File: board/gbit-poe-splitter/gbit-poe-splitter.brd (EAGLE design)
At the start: 100 x 80 mm, 51 parts, among them IC1 LM2596HVS, U1 TPS2379DDA

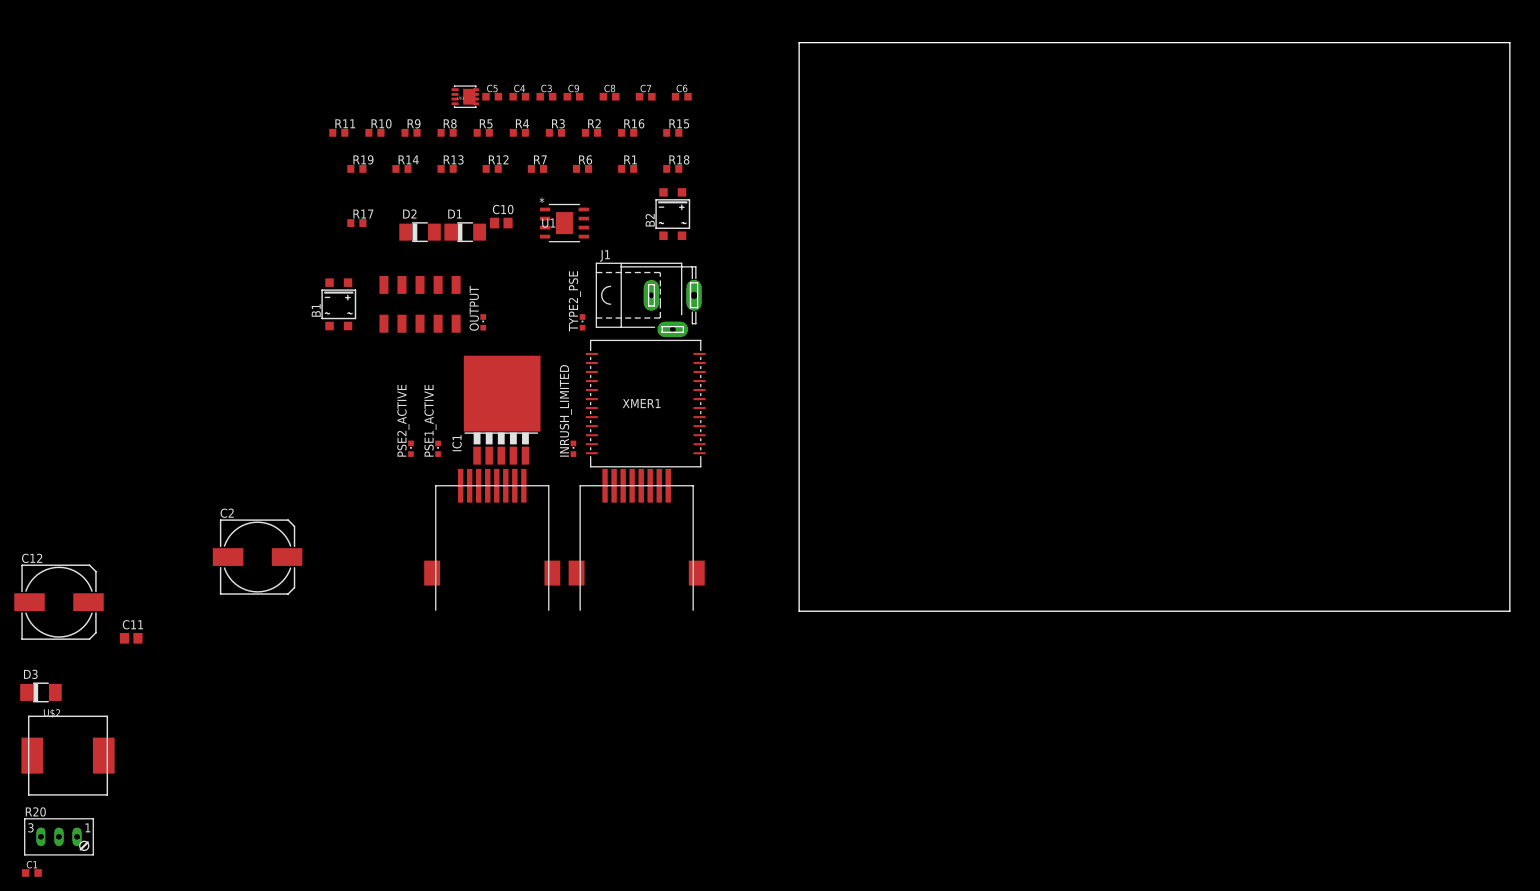
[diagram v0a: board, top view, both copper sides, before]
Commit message: Began the routing process
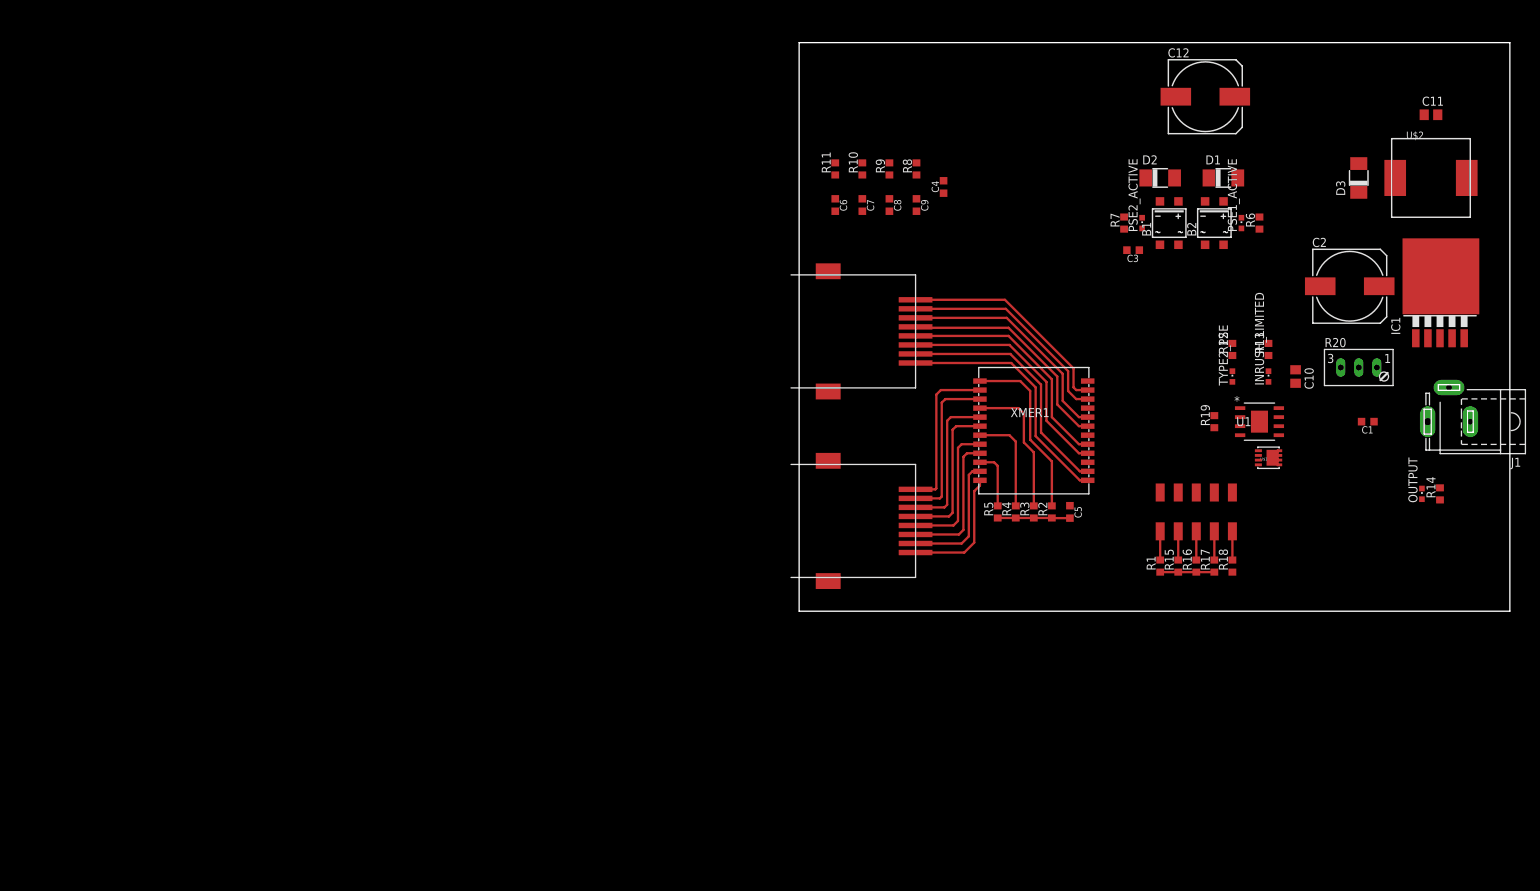
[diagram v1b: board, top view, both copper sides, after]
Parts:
- moved U$2 208.3 mm to (88.9, 61.0)
- moved D3 199.0 mm to (78.7, 61.0), turned to 90 degrees
- moved C1 198.4 mm to (80.0, 26.7), turned to 180 degrees
- moved C11 197.2 mm to (88.9, 69.8)
- moved R20 194.4 mm to (78.7, 33.0)
- moved C12 176.3 mm to (57.1, 72.4)
- moved C2 158.3 mm to (77.5, 45.7)
- moved R14 153.0 mm to (90.2, 16.5), turned to 90 degrees
- moved OUTPUT 134.3 mm to (87.6, 16.5)
- moved IC1 133.1 mm to (90.2, 44.5)
- moved R17 129.9 mm to (58.4, 6.35), turned to 90 degrees
- moved R19 125.8 mm to (58.4, 26.7), turned to 90 degrees
- moved U$1 123.9 mm to (66.0, 21.6)
- moved R13 118.3 mm to (66.0, 36.8), turned to 90 degrees
- moved PSE1_ACTIVE 117.4 mm to (62.2, 54.6)
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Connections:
- net GND: now also ETH-IN.S2, ETH-OUT.S2
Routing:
- net N$9: track 0.00 -> 35.1 mm
- net N$10: track 0.00 -> 35.0 mm
- net N$11: track 0.00 -> 33.7 mm
- net N$12: track 0.00 -> 33.7 mm
- net N$13: track 0.00 -> 32.3 mm
- net N$14: track 0.00 -> 32.2 mm
- net N$15: track 0.00 -> 31.1 mm
- net N$16: track 0.00 -> 31.0 mm
- net PD1A: track 0.00 -> 25.1 mm
- net N$2: track 0.00 -> 22.6 mm
- net N$1: track 0.00 -> 22.6 mm
- net N$4: track 0.00 -> 21.3 mm
- net N$3: track 0.00 -> 21.2 mm
- net PD1B: track 0.00 -> 20.1 mm
- net N$6: track 0.00 -> 19.8 mm
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
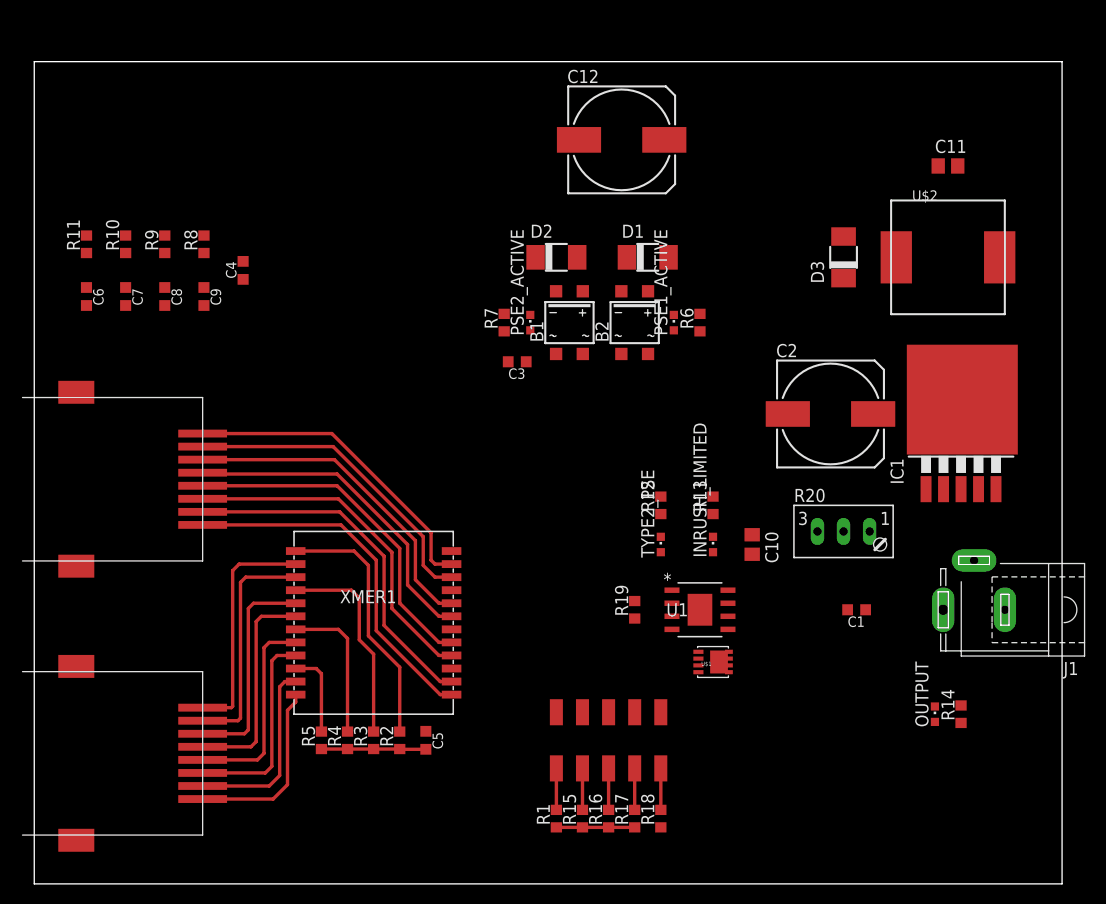
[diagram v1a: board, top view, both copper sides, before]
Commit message: Routed top side of the board completely
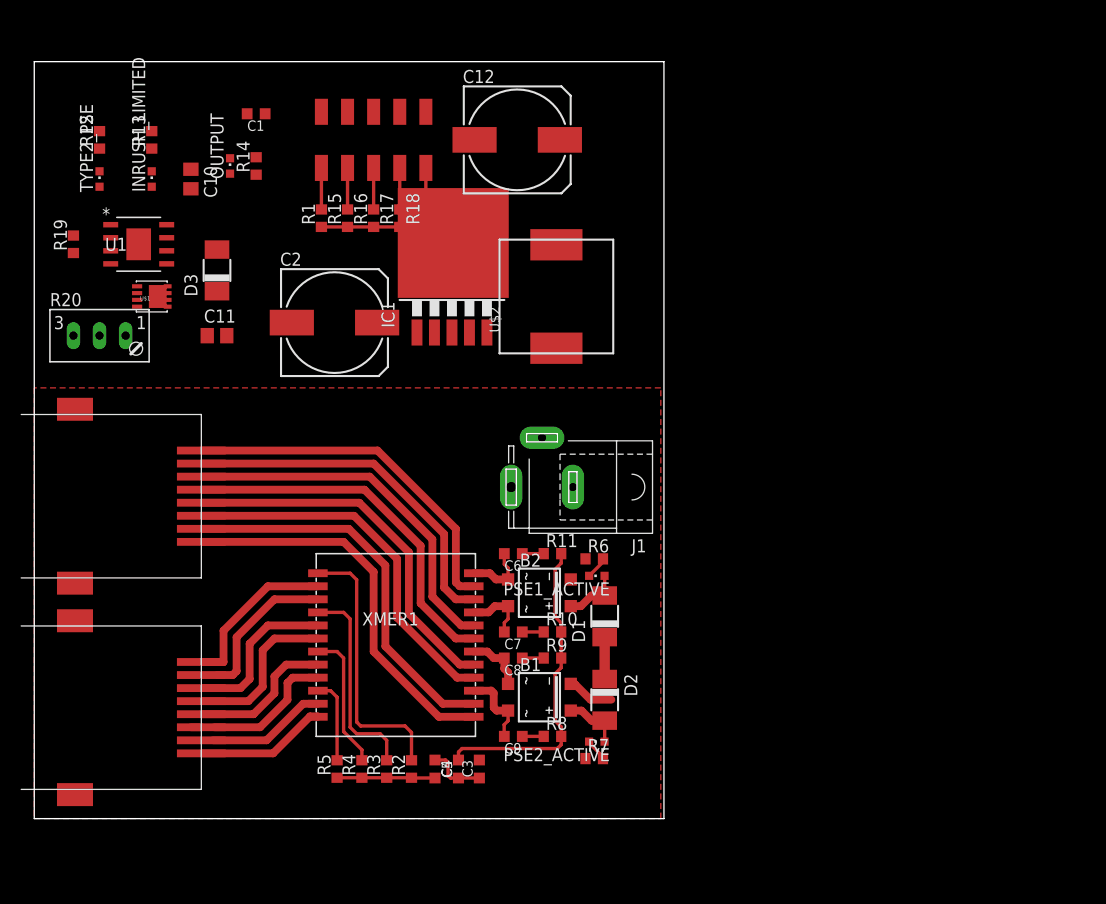
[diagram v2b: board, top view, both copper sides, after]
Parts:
- moved OUTPUT 86.9 mm to (19.1, 69.8)
- moved R14 86.9 mm to (21.6, 69.8)
- moved C1 75.8 mm to (21.6, 74.9)
- moved R20 74.9 mm to (6.35, 52.1)
- moved C11 73.0 mm to (17.8, 53.3)
- moved INRUSH_LIMITED 65.2 mm to (11.4, 68.6)
- moved R12 65.2 mm to (6.35, 72.4)
- moved R13 65.2 mm to (11.4, 72.4)
- moved R19 65.2 mm to (3.81, 62.2)
- moved TYPE2_PSE 65.2 mm to (6.35, 68.6)
- moved U$1 65.2 mm to (11.4, 57.1)
- moved U1 65.2 mm to (10.2, 62.2)
- moved C10 65.2 mm to (15.2, 68.6)
- moved R15 62.7 mm to (30.5, 64.8)
- moved CLASS-SEL 62.7 mm to (33.0, 72.4)
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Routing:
- net N$19: track 0.00 -> 30.6 mm
- net N$2: track 22.6 -> 14.8 mm
- net PSE2B: track 0.00 -> 7.63 mm
- net N$7: track 18.3 -> 11.7 mm
- net N$1: track 22.6 -> 16.2 mm
- net PSE1B: track 0.00 -> 6.25 mm
- net PSE1A: track 0.00 -> 6.25 mm
- net PSE1: track 0.00 -> 6.00 mm
- net PSE2A: track 0.00 -> 5.92 mm
- net N$17: track 0.00 -> 5.79 mm
- net N$6: track 19.8 -> 14.1 mm
- net PSE2: track 0.00 -> 5.75 mm
- net N$5: track 19.8 -> 14.3 mm
- net N$3: track 21.2 -> 15.9 mm
- net N$4: track 21.3 -> 15.9 mm
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- added copper zone on layer 1, net GND
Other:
- board size 100 x 80 mm -> 61.3 x 73.7 mm

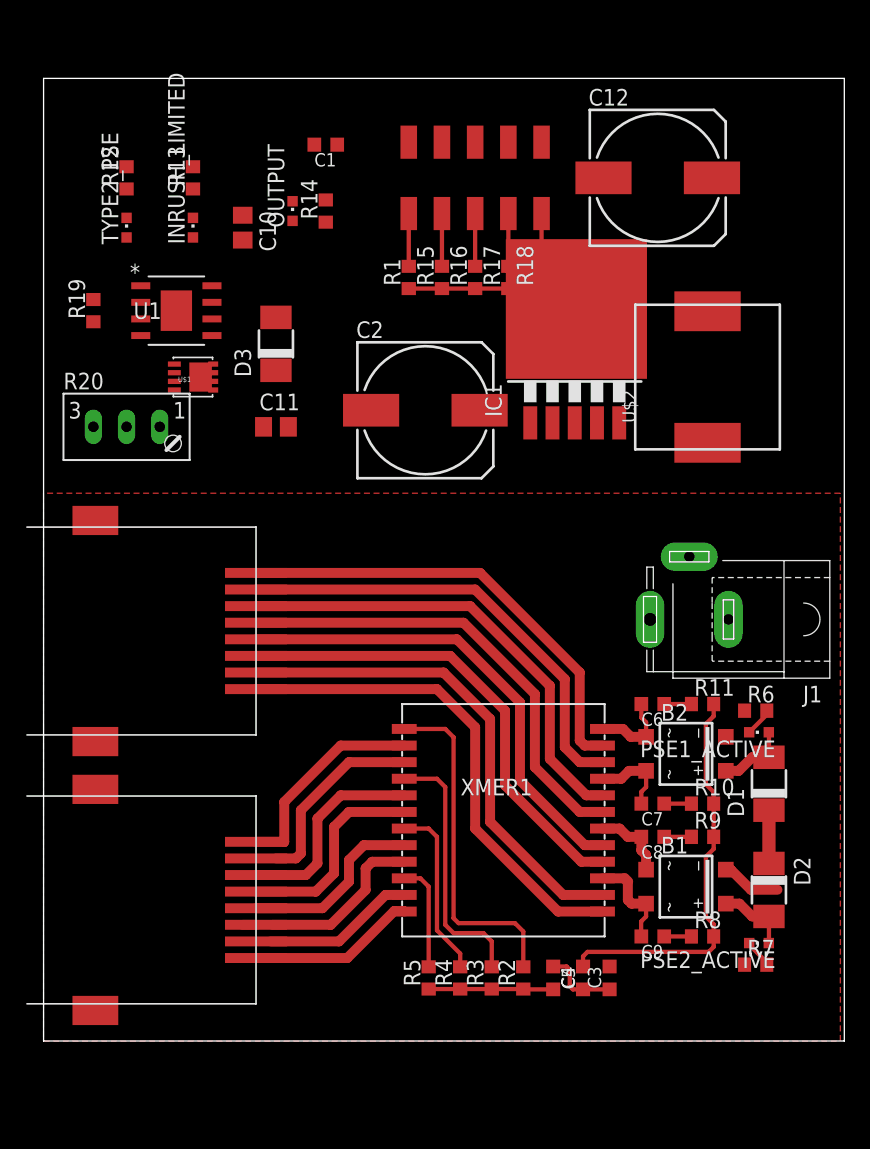
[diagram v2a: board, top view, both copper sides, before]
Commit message: Completed board layout
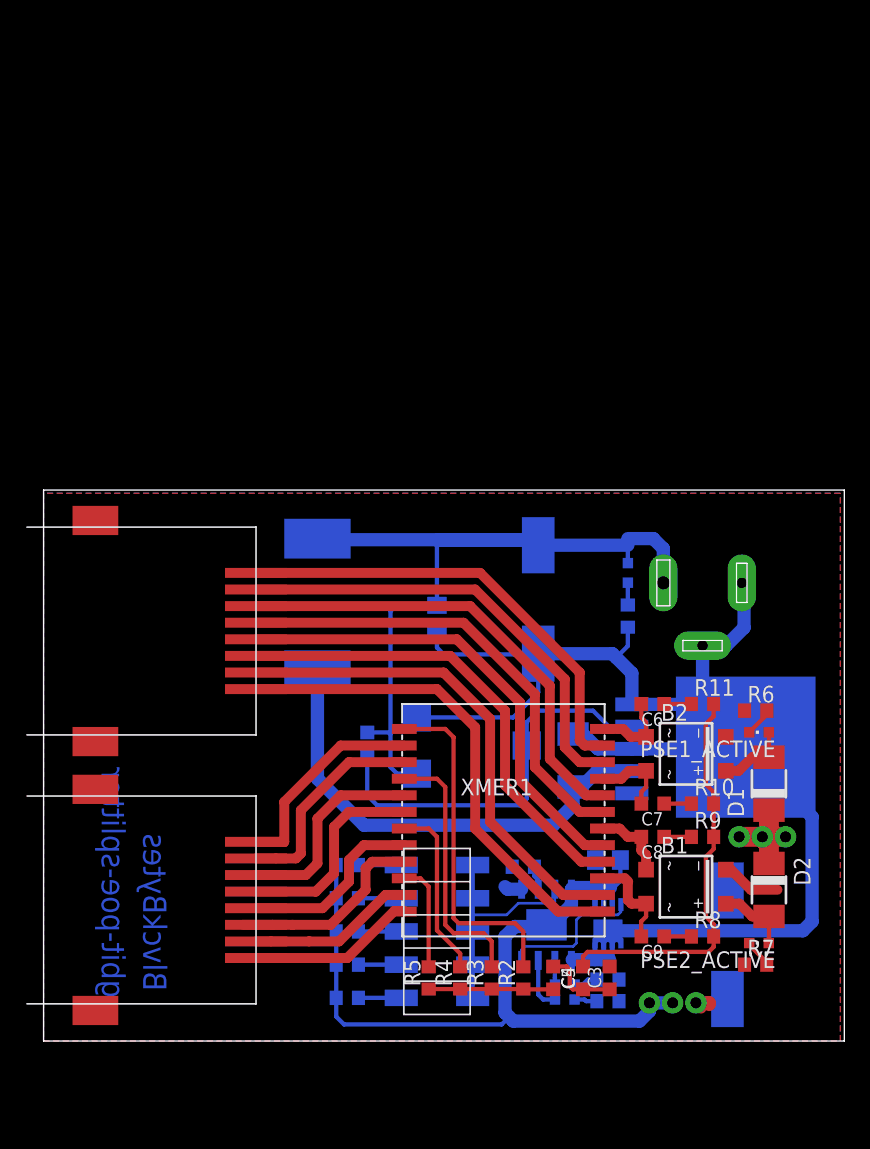
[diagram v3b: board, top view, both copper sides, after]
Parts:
- removed R20: (no value), pot:S64W
- added U$3: TRIM_CA6_VSMD, TRIM_CA6_VSMD:TRIM_CA6_VSMD
- moved R12 73.0 mm to (43.2, 9.40), flipped to the bottom, turned to 0 degrees
- moved R13 69.1 mm to (43.2, 11.0), flipped to the bottom, turned to 0 degrees
- moved TYPE2_PSE 67.9 mm to (39.9, 9.53), flipped to the bottom, turned to 270 degrees
- moved INRUSH_LIMITED 64.5 mm to (39.9, 10.7), flipped to the bottom, turned to 270 degrees
- moved C12 58.9 mm to (52.3, 13.7), flipped to the bottom, turned to 90 degrees
- moved CLASS-SEL 57.7 mm to (30.1, 14.7), flipped to the bottom, turned to 90 degrees
- moved C10 55.9 mm to (43.2, 20.2), flipped to the bottom, turned to 180 degrees
- moved R1 55.3 mm to (23.2, 9.65), flipped to the bottom, turned to 180 degrees
- moved U1 54.9 mm to (38.5, 15.2), flipped to the bottom, turned to 270 degrees
- moved R19 53.8 mm to (36.7, 19.7), flipped to the bottom, turned to 180 degrees
- moved R15 53.1 mm to (23.2, 12.2), flipped to the bottom, turned to 180 degrees
- moved U$1 52.5 mm to (43.2, 15.4), flipped to the bottom, turned to 270 degrees
- moved R16 51.0 mm to (23.2, 14.7), flipped to the bottom, turned to 180 degrees
- moved R17 49.1 mm to (23.2, 17.3), flipped to the bottom, turned to 180 degrees
- moved R18 47.3 mm to (23.2, 19.8), flipped to the bottom, turned to 180 degrees
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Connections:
- net GND: no longer R14.1
- net N$37: now also U$3.3; no longer R20.S
- net POWER: now also U$3.1; no longer R20.A
- net RTN: now also IC1.6, R14.1, U$3.2; no longer R20.E
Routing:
- net RTN: track 0.00 -> 117.0 mm
- net POWER: track 0.00 -> 64.1 mm
- net GND: track 12.2 -> 70.9 mm, vias 0 -> 3
- net N$34: track 0.00 -> 36.4 mm
- net N$37: track 0.00 -> 30.5 mm
- net R_CLS: track 0.00 -> 17.8 mm
- net PSE: track 4.08 -> 17.5 mm, vias 0 -> 3
- net N$35: track 0.00 -> 11.2 mm
- net T2P: track 0.00 -> 4.05 mm
- net N$27: track 0.00 -> 1.86 mm
- net CDB: track 0.00 -> 1.85 mm
- net N$36: track 0.00 -> 1.84 mm
- net N$26: track 0.00 -> 1.75 mm
- net N$28: track 0.00 -> 1.70 mm
- net N$2: track 14.8 -> 16.3 mm
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- added copper zone on layer 16, net PSE
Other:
- board size 61.3 x 73.7 mm -> 61.3 x 42.2 mm
- board text added: "BlvckBytes"
- board text added: "gbit-poe-splitter"
